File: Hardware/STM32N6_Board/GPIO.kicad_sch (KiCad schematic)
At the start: 13 parts, among them U1 STM32N657I0H3Q, Y1 32.768kHz, Y3 48MHz

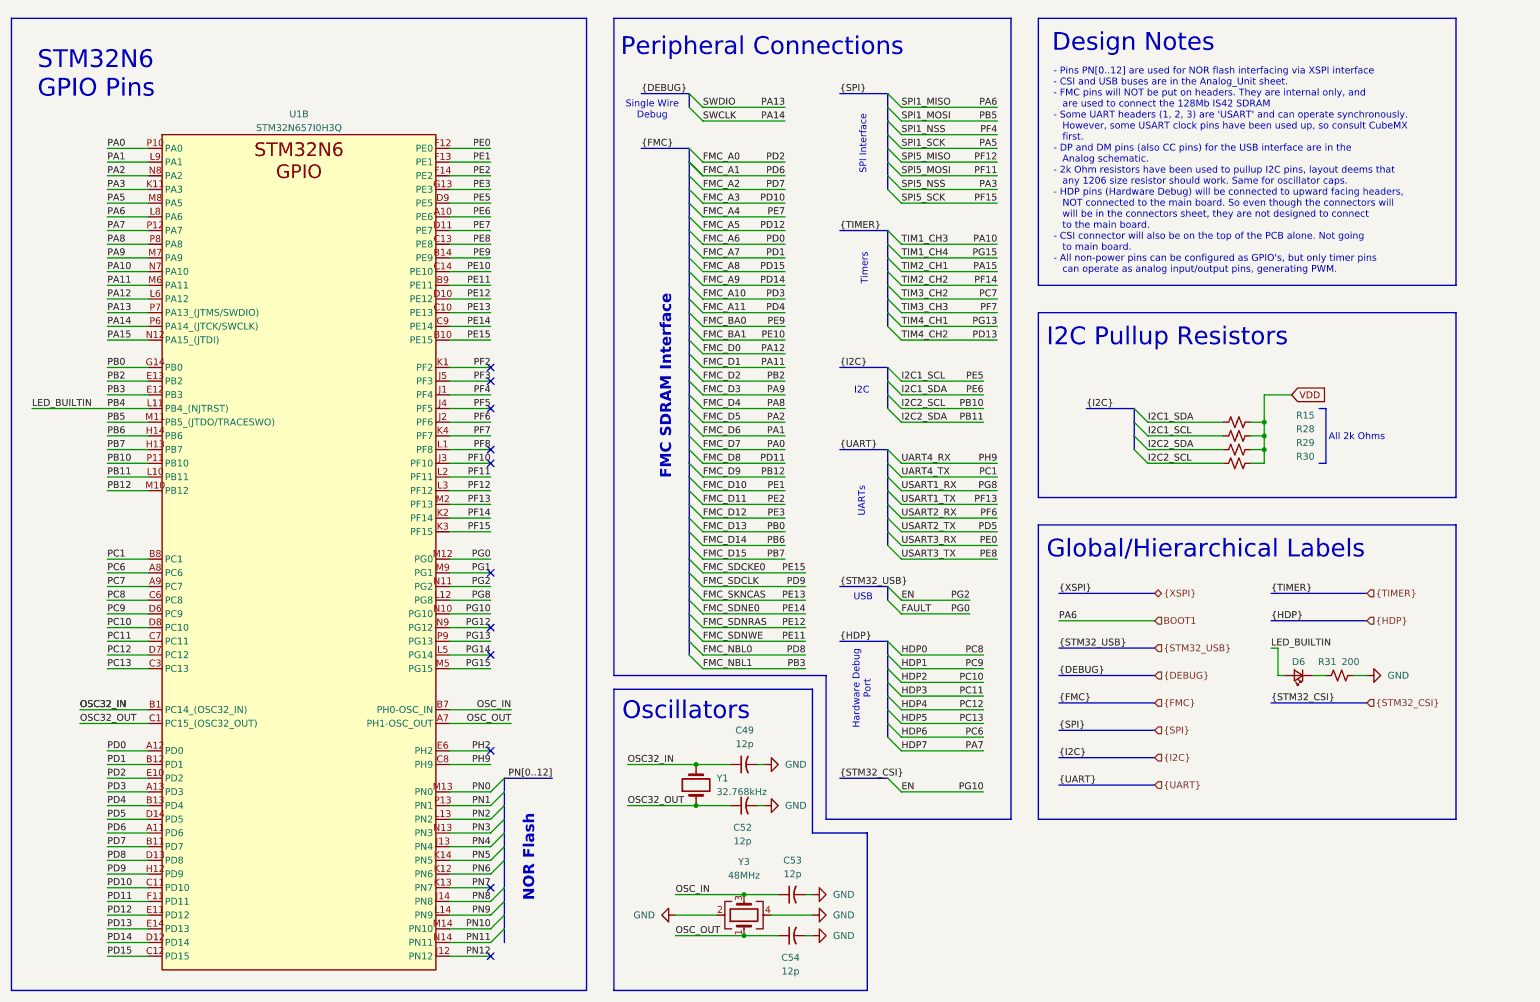
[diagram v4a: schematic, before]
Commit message: Completed schematic layout, ERC check, and footprint assignment
- Completed and checked the schematic layout
- Ran the ERC check; no errors (but lots of (checked) warnings)
- Assigned footprints. Most in std lib, others in footprints.pretty
- Imported the components to the PCB Editor, and fixed errors
- All that's left is PCB layout!
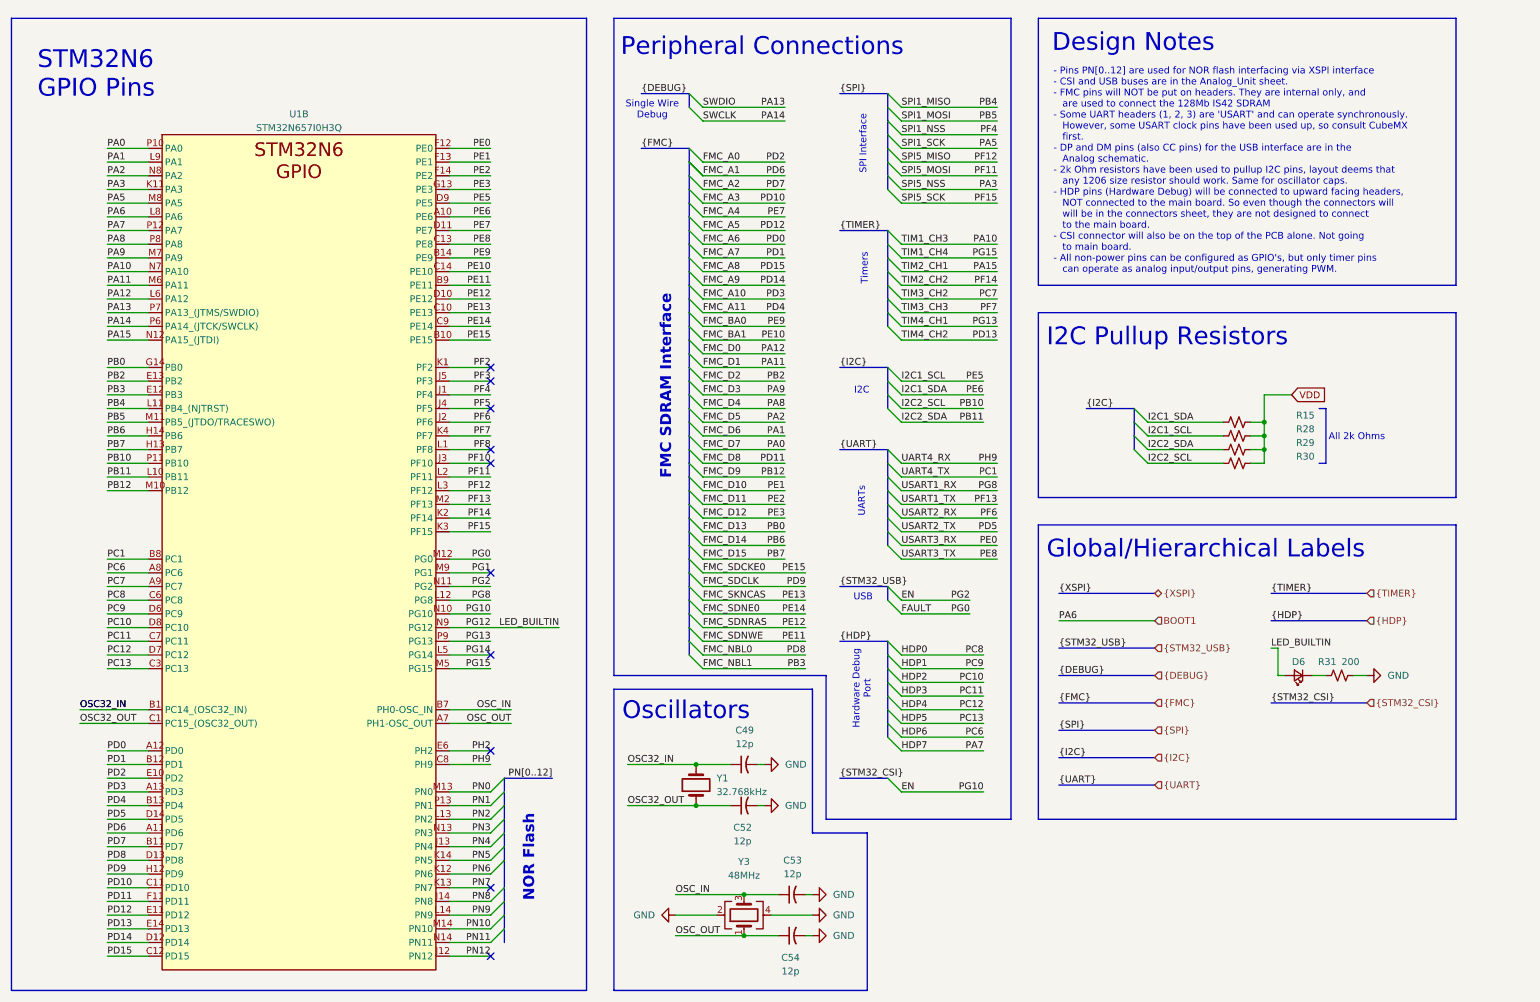
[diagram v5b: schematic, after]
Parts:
- C49, C52, C53, C54: footprint (none) -> Capacitor_SMD:C_0402_1005Metric_Pad0.74x0.62mm_HandSolder
- D6: footprint (none) -> LED_SMD:LED_0603_1608Metric_Pad1.05x0.95mm_HandSolder
- R15, R28, R29, R30, R31: footprint (none) -> Resistor_SMD:R_0805_2012Metric_Pad1.20x1.40mm_HandSolder
- U1: footprint (none) -> STM32N6_Footprints:STM32N657I0H3Q_VFBGA178_14x14
- Y1: footprint (none) -> STM32N6_Footprints:32kHz_SC-20S_2Pin_2.05x1.2mm
- Y3: footprint (none) -> STM32N6_Footprints:48MHz_Q22FA12800150_4Pin_2.0z1.6mm
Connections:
- net PG12 is gone; now on net LED_BUILTIN: U1.N9 (PG12)
- net LED_BUILTIN: no longer U1.L11 (PB4_(NJTRST))
- new net PB4: U1.L11 (PB4_(NJTRST))
- no-connect marks 11 -> 10
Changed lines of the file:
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@@
 	)
 	(no_connect
-		(at 104.14 128.27)
-	)
-	(no_connect
 		(at 104.14 151.13)
 	)
@@
 	(wire
 		(pts
-			(xy 19.05 87.63) (xy 40.64 87.63)
-		)
-		(stroke
-			(width 0)
-			(type default)
-		)
-	)
-	(wire
-		(pts
 			(xy 33.02 130.81) (xy 40.64 130.81)
 		)
@@
 		)
 	)
+	(wire
+		(pts
+			(xy 33.02 87.63) (xy 40.64 87.63)
+		)
+		(stroke
+			(width 0)
+			(type default)
+		)
+	)
 	(bus
 		(pts
@@
 	(wire
 		(pts
-			(xy 96.52 128.27) (xy 104.14 128.27)
+			(xy 96.52 128.27) (xy 116.84 128.27)
 		)
 		(stroke
@@
 		)
 	)
-	(label "PA6"
+	(label "PB4"
 		(at 198.12 31.75 180)
 		(effects
@@
 	)
 	(label "LED_BUILTIN"
-		(at 19.05 87.63 0)
+		(at 116.84 128.27 180)
 		(effects
 			(font
 				(size 1.27 1.27)
 			)
-			(justify left bottom)
+			(justify right bottom)
 		)
 	)
@@
 			)
 		)
-		(property "Footprint" ""
+		(property "Footprint" "Resistor_SMD:R_0805_2012Metric_Pad1.20x1.40mm_HandSolder"
 			(at 242.57 95.25 0)
 			(effects
@@
 			)
 		)
-		(property "Footprint" ""
+		(property "Footprint" "Capacitor_SMD:C_0402_1005Metric_Pad0.74x0.62mm_HandSolder"
 			(at 151.13 153.67 0)
 			(effects
@@
 			)
 		)
-		(property "Footprint" ""
+		(property "Footprint" "Capacitor_SMD:C_0402_1005Metric_Pad0.74x0.62mm_HandSolder"
 			(at 160.02 177.8 0)
 			(effects
@@
 			)
 		)
-		(property "Footprint" ""
+		(property "Footprint" "Resistor_SMD:R_0805_2012Metric_Pad1.20x1.40mm_HandSolder"
 			(at 242.57 97.79 0)
 			(effects
@@
 			)
 		)
-		(property "Footprint" ""
+		(property "Footprint" "STM32N6_Footprints:STM32N657I0H3Q_VFBGA178_14x14"
 			(at 68.58 40.64 0)
 			(effects
@@
 			)
 		)
-		(property "Footprint" ""
+		(property "Footprint" "STM32N6_Footprints:48MHz_Q22FA12800150_4Pin_2.0z1.6mm"
 			(at 151.13 181.61 0)
 			(effects
@@
 			)
 		)
-		(property "Footprint" ""
+		(property "Footprint" "Resistor_SMD:R_0805_2012Metric_Pad1.20x1.40mm_HandSolder"
 			(at 242.57 92.71 0)
 			(effects
@@
 			)
 		)
-		(property "Footprint" ""
+		(property "Footprint" "Resistor_SMD:R_0805_2012Metric_Pad1.20x1.40mm_HandSolder"
 			(at 261.62 137.16 0)
 			(effects
@@
 			)
 		)
-		(property "Footprint" ""
+		(property "Footprint" "LED_SMD:LED_0603_1608Metric_Pad1.05x0.95mm_HandSolder"
 			(at 254 137.16 90)
 			(effects
@@
 			)
 		)
-		(property "Footprint" ""
+		(property "Footprint" "Capacitor_SMD:C_0402_1005Metric_Pad0.74x0.62mm_HandSolder"
 			(at 151.13 161.29 0)
 			(effects
@@
 			)
 		)
-		(property "Footprint" ""
+		(property "Footprint" "STM32N6_Footprints:32kHz_SC-20S_2Pin_2.05x1.2mm"
 			(at 142.24 157.48 0)
 			(effects
@@
 			)
 		)
-		(property "Footprint" ""
+		(property "Footprint" "Capacitor_SMD:C_0402_1005Metric_Pad0.74x0.62mm_HandSolder"
 			(at 160.02 185.42 0)
 			(effects
@@
 			)
 		)
-		(property "Footprint" ""
+		(property "Footprint" "Resistor_SMD:R_0805_2012Metric_Pad1.20x1.40mm_HandSolder"
 			(at 242.57 90.17 0)
 			(effects

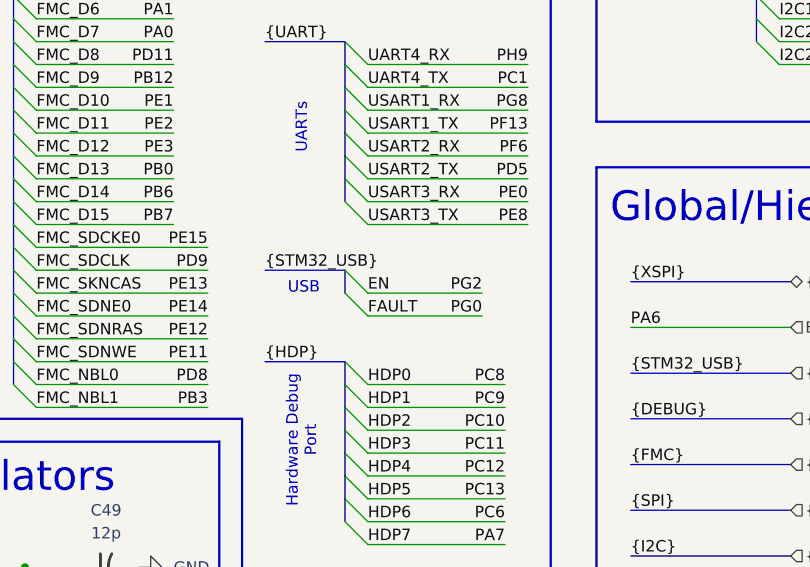
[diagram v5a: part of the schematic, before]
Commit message: Completed a lot of the layout of the STM Board
- Major layout complete, but all the wiring still left. 488 open nets!
- The STM32's BGA fanout is complete, now comes laying out traces
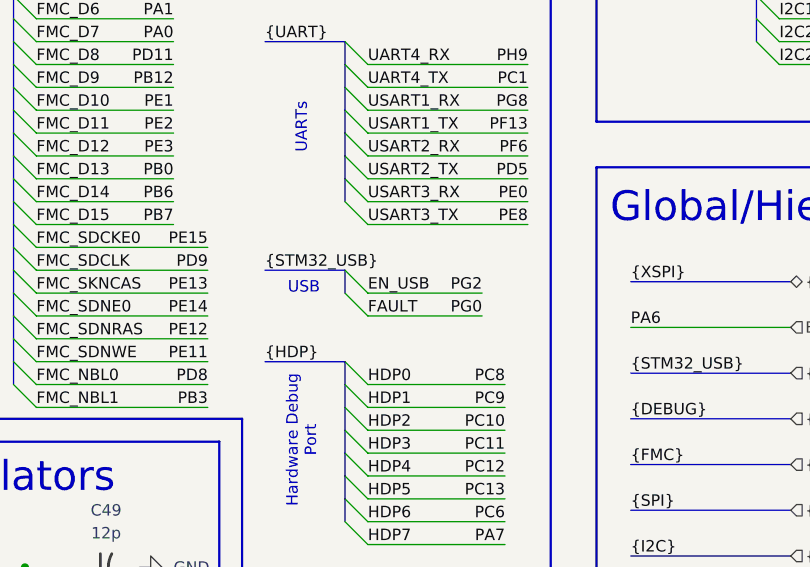
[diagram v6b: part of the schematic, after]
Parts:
- R15, R28, R29, R30: footprint Resistor_SMD:R_0805_2012Metric_Pad1.20x1.40mm_HandSolder -> Resistor_SMD:R_0402_1005Metric
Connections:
- net EN: no longer U1.N11 (PG2)
- new net EN_USB: U1.N11 (PG2)
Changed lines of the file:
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@@
 	(wire
 		(pts
+			(xy 143.51 97.79) (xy 158.75 97.79)
+		)
+		(stroke
+			(width 0)
+			(type default)
+		)
+	)
+	(wire
+		(pts
 			(xy 143.51 128.27) (xy 162.56 128.27)
 		)
@@
 		)
 	)
+	(wire
+		(pts
+			(xy 143.51 110.49) (xy 158.75 110.49)
+		)
+		(stroke
+			(width 0)
+			(type default)
+		)
+	)
 	(bus
 		(pts
@@
 		)
 	)
-	(wire
-		(pts
-			(xy 143.51 92.71) (xy 158.75 92.71)
-		)
-		(stroke
-			(width 0)
-			(type default)
-		)
-	)
 	(bus
 		(pts
@@
 	(wire
 		(pts
-			(xy 143.51 115.57) (xy 158.75 115.57)
-		)
-		(stroke
-			(width 0)
-			(type default)
-		)
-	)
-	(wire
-		(pts
-			(xy 143.51 113.03) (xy 158.75 113.03)
-		)
-		(stroke
-			(width 0)
-			(type default)
-		)
-	)
-	(wire
-		(pts
 			(xy 143.51 72.39) (xy 158.75 72.39)
 		)
@@
 	(wire
 		(pts
-			(xy 143.51 110.49) (xy 158.75 110.49)
-		)
-		(stroke
-			(width 0)
-			(type default)
-		)
-	)
-	(wire
-		(pts
 			(xy 96.52 135.89) (xy 104.14 135.89)
 		)
@@
 	(wire
 		(pts
-			(xy 143.51 97.79) (xy 158.75 97.79)
-		)
-		(stroke
-			(width 0)
-			(type default)
-		)
-	)
-	(wire
-		(pts
 			(xy 104.14 49.53) (xy 96.52 49.53)
 		)
@@
 		)
 	)
-	(wire
-		(pts
-			(xy 143.51 87.63) (xy 158.75 87.63)
-		)
-		(stroke
-			(width 0)
-			(type default)
-		)
-	)
 	(bus
 		(pts
@@
 	(wire
 		(pts
+			(xy 143.51 100.33) (xy 158.75 100.33)
+		)
+		(stroke
+			(width 0)
+			(type default)
+		)
+	)
+	(wire
+		(pts
+			(xy 143.51 107.95) (xy 158.75 107.95)
+		)
+		(stroke
+			(width 0)
+			(type default)
+		)
+	)
+	(wire
+		(pts
 			(xy 33.02 118.11) (xy 40.64 118.11)
 		)
@@
 		)
 	)
-	(wire
-		(pts
-			(xy 143.51 105.41) (xy 158.75 105.41)
-		)
-		(stroke
-			(width 0)
-			(type default)
-		)
-	)
 	(bus
 		(pts
@@
 		)
 	)
+	(wire
+		(pts
+			(xy 143.51 105.41) (xy 158.75 105.41)
+		)
+		(stroke
+			(width 0)
+			(type default)
+		)
+	)
 	(bus
 		(pts
@@
 		)
 	)
+	(wire
+		(pts
+			(xy 143.51 115.57) (xy 158.75 115.57)
+		)
+		(stroke
+			(width 0)
+			(type default)
+		)
+	)
 	(bus
 		(pts
@@
 	(wire
 		(pts
+			(xy 143.51 85.09) (xy 158.75 85.09)
+		)
+		(stroke
+			(width 0)
+			(type default)
+		)
+	)
+	(wire
+		(pts
 			(xy 96.52 110.49) (xy 104.14 110.49)
 		)
@@
 	(wire
 		(pts
+			(xy 143.51 90.17) (xy 158.75 90.17)
+		)
+		(stroke
+			(width 0)
+			(type default)
+		)
+	)
+	(wire
+		(pts
 			(xy 33.02 100.33) (xy 40.64 100.33)
 		)
@@
 		)
 	)
+	(wire
+		(pts
+			(xy 143.51 87.63) (xy 158.75 87.63)
+		)
+		(stroke
+			(width 0)
+			(type default)
+		)
+	)
 	(bus
 		(pts
@@
 	(wire
 		(pts
+			(xy 143.51 102.87) (xy 158.75 102.87)
+		)
+		(stroke
+			(width 0)
+			(type default)
+		)
+	)
+	(wire
+		(pts
 			(xy 96.52 146.05) (xy 107.95 146.05)
 		)
@@
 	(wire
 		(pts
-			(xy 143.51 102.87) (xy 158.75 102.87)
-		)
-		(stroke
-			(width 0)
-			(type default)
-		)
-	)
-	(wire
-		(pts
 			(xy 104.14 85.09) (xy 96.52 85.09)
 		)
@@
 	(wire
 		(pts
-			(xy 143.51 100.33) (xy 158.75 100.33)
+			(xy 143.51 92.71) (xy 158.75 92.71)
 		)
 		(stroke
@@
 	(wire
 		(pts
+			(xy 143.51 113.03) (xy 158.75 113.03)
+		)
+		(stroke
+			(width 0)
+			(type default)
+		)
+	)
+	(wire
+		(pts
 			(xy 104.14 171.45) (xy 96.52 171.45)
 		)
@@
 	(wire
 		(pts
-			(xy 143.51 85.09) (xy 158.75 85.09)
-		)
-		(stroke
-			(width 0)
-			(type default)
-		)
-	)
-	(wire
-		(pts
 			(xy 143.51 120.65) (xy 162.56 120.65)
 		)
@@
 		)
 	)
-	(wire
-		(pts
-			(xy 143.51 95.25) (xy 158.75 95.25)
-		)
-		(stroke
-			(width 0)
-			(type default)
-		)
-	)
 	(bus
 		(pts
@@
 	(wire
 		(pts
+			(xy 143.51 95.25) (xy 158.75 95.25)
+		)
+		(stroke
+			(width 0)
+			(type default)
+		)
+	)
+	(wire
+		(pts
 			(xy 27.94 143.51) (xy 40.64 143.51)
 		)
@@
 		)
 	)
-	(wire
-		(pts
-			(xy 143.51 90.17) (xy 158.75 90.17)
-		)
-		(stroke
-			(width 0)
-			(type default)
-		)
-	)
 	(bus
 		(pts
@@
 	(wire
 		(pts
-			(xy 143.51 107.95) (xy 158.75 107.95)
-		)
-		(stroke
-			(width 0)
-			(type default)
-		)
-	)
-	(wire
-		(pts
 			(xy 180.34 62.23) (xy 198.12 62.23)
 		)
@@
 		)
 	)
-	(label "EN"
+	(label "EN_USB"
 		(at 180.34 123.19 0)
 		(effects
@@
 			)
 		)
-		(property "Footprint" "Resistor_SMD:R_0805_2012Metric_Pad1.20x1.40mm_HandSolder"
+		(property "Footprint" "Resistor_SMD:R_0402_1005Metric"
 			(at 242.57 95.25 0)
 			(effects
@@
 			)
 		)
-		(property "Footprint" "Resistor_SMD:R_0805_2012Metric_Pad1.20x1.40mm_HandSolder"
+		(property "Footprint" "Resistor_SMD:R_0402_1005Metric"
 			(at 242.57 97.79 0)
 			(effects
@@
 			)
 		)
-		(property "Footprint" "Resistor_SMD:R_0805_2012Metric_Pad1.20x1.40mm_HandSolder"
+		(property "Footprint" "Resistor_SMD:R_0402_1005Metric"
 			(at 242.57 92.71 0)
 			(effects
@@
 			)
 		)
-		(property "Footprint" "Resistor_SMD:R_0805_2012Metric_Pad1.20x1.40mm_HandSolder"
+		(property "Footprint" "Resistor_SMD:R_0402_1005Metric"
 			(at 242.57 90.17 0)
 			(effects

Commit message: almost finished with the board
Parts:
- R31: footprint Resistor_SMD:R_0805_2012Metric_Pad1.20x1.40mm_HandSolder -> Resistor_SMD:R_0402_1005Metric
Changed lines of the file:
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@@
 			)
 		)
-		(property "Footprint" "Resistor_SMD:R_0805_2012Metric_Pad1.20x1.40mm_HandSolder"
+		(property "Footprint" "Resistor_SMD:R_0402_1005Metric"
 			(at 261.62 137.16 0)
 			(effects
